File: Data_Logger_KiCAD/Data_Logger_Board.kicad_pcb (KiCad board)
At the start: 6 copper layers, 45 x 63 mm, 105 parts, among them J1 USB_C_Receptacle_USB2.0_16P, J2 Screw_Terminal_01x02, J3 Micro_SD_Card, J4 Conn_Coaxial_Small, J5 Conn_01x02, Q1 Q_NMOS_GSD, SW1 SW_Push, SW2 SW_Push, U1 LSM6DSO32TR, U10 BMP390L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

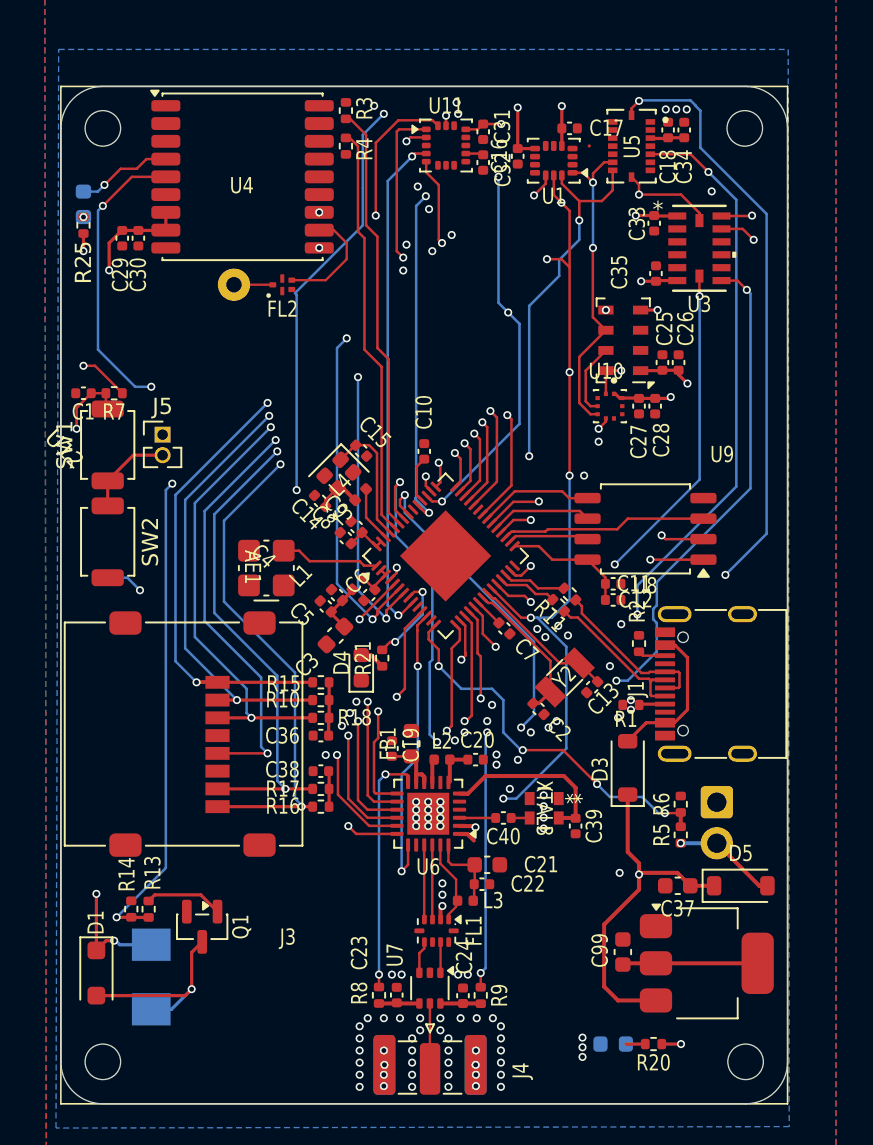
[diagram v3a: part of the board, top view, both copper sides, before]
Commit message: finish SPI routing +silkscreen tidy
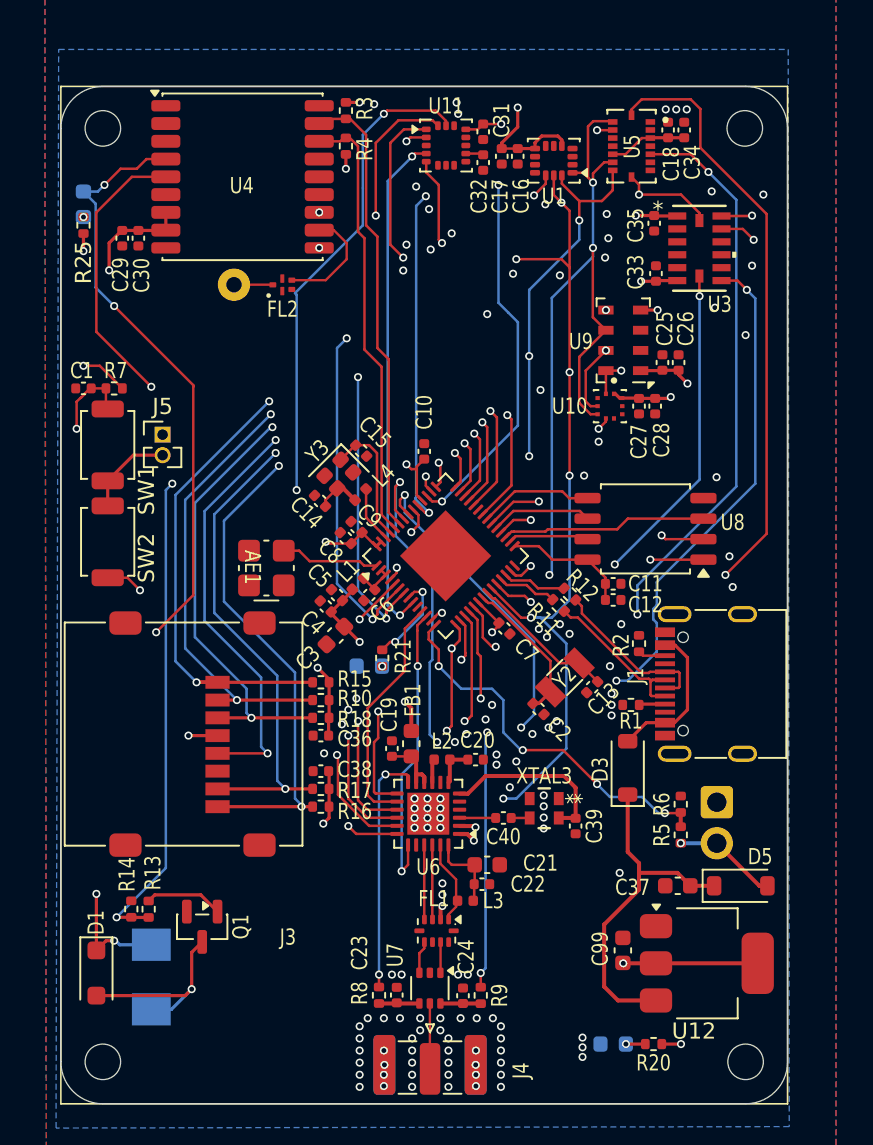
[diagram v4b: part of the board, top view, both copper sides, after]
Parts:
- D4: moved to B.Cu
- moved C17 4.54 mm to (147.3, 51.4), turned to -90 degrees
- moved D4 0.51 mm to (139.1, 83.0), turned to 0 degrees
- moved C1 0.30 mm to (121.4, 65.8)
- moved R7 0.30 mm to (123.3, 65.8)
- moved C99 0.10 mm to (154.8, 100.6)
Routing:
- net /MCU/TIMEPULSE: track 6.08 -> 56.2 mm, vias 1 -> 4
- net /MCU/MISO: track 67.7 -> 101.9 mm, vias 6 -> 8
- net +3V3: track 69.2 -> 85.0 mm, vias 14 -> 24
- net /MCU/MAG_INT: track 31.6 -> 42.3 mm
- net /MCU/MOSI: track 104.5 -> 109.3 mm, vias 7 -> 9
- net /MCU/~{ACCEL_CS}: track 35.9 -> 32.6 mm
- net /MCU/SCL: track 26.6 -> 28.3 mm
- net /MCU/SDA: track 25.5 -> 27.3 mm
- net Net-(D4-A): track 1.59 -> 0.00 mm, vias 0 -> 1
- net /MCU/RADIO_BUSY: track 15.8 -> 14.8 mm, vias 2 -> 0
- net /MCU/PWR_IN: track 21.7 -> 22.4 mm, vias 1 -> 0
- net /MCU/~{RESET}: track 32.1 -> 32.8 mm
- net /MCU/GPS_EXTINT: track 48.2 -> 47.7 mm, vias 3 -> 2
- net /MCU/ACCEL_INT: vias 3 -> 2
- net Net-(U6-VBAT): vias 0 -> 1
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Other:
- board text added: "R12"

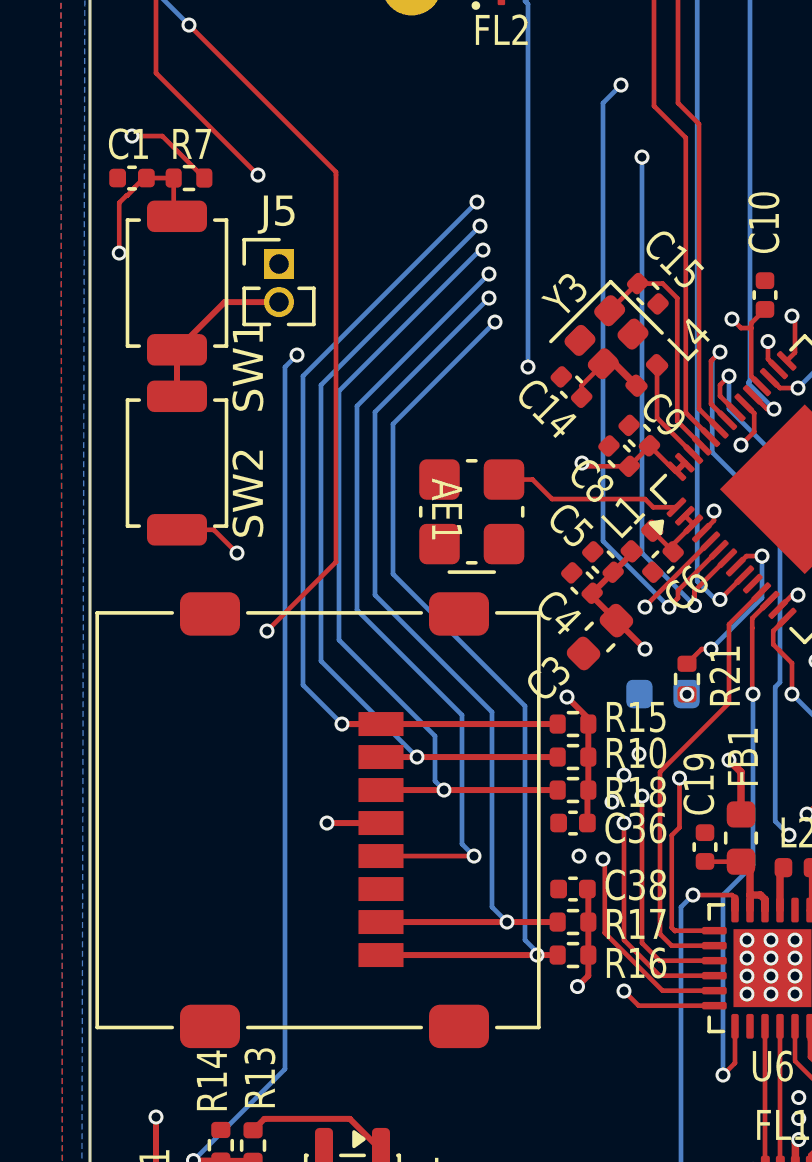
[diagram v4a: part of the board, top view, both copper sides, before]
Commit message: add stitching vias
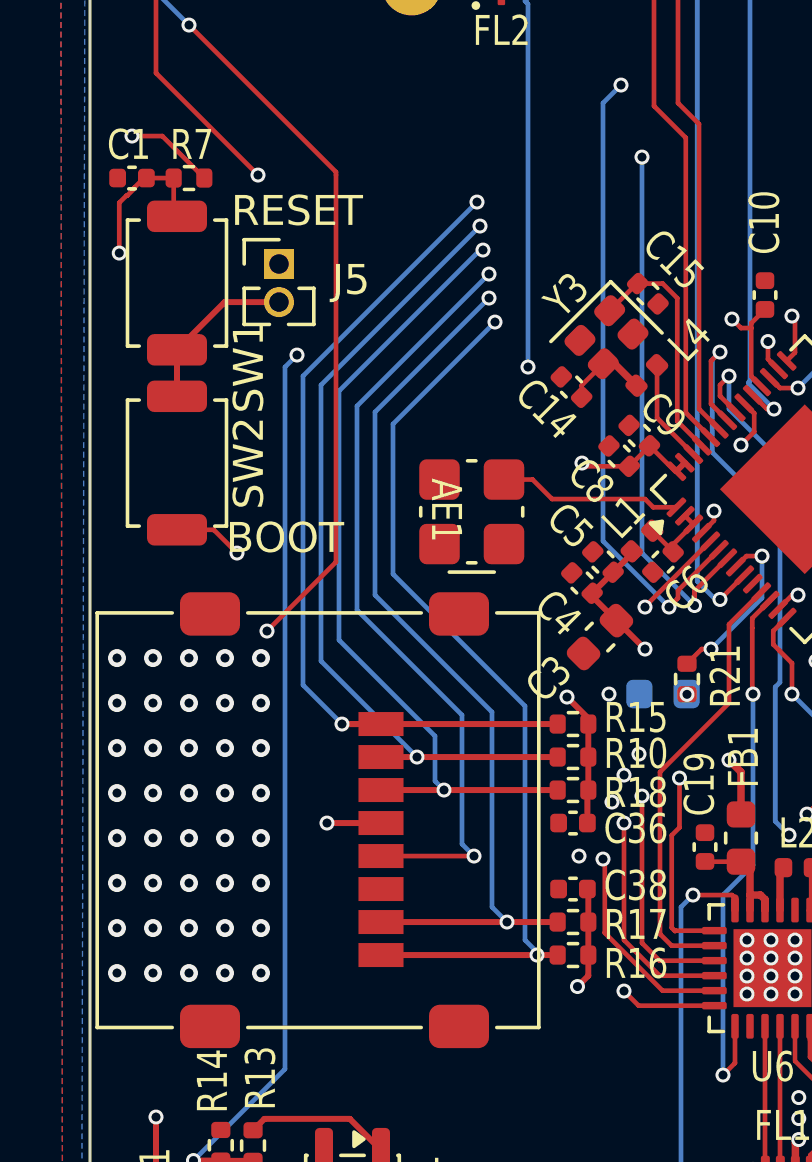
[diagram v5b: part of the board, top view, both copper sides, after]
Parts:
- added REF**: aiaa-mask-silk-8x4, beavs-footprints:aiaa-mask-silk-8x4, B.Cu at (132.3, 106.6)
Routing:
- net GND: vias 124 -> 165
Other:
- board text added: "ASDT"
- board text added: "BOOT"
- board text added: "RESET"

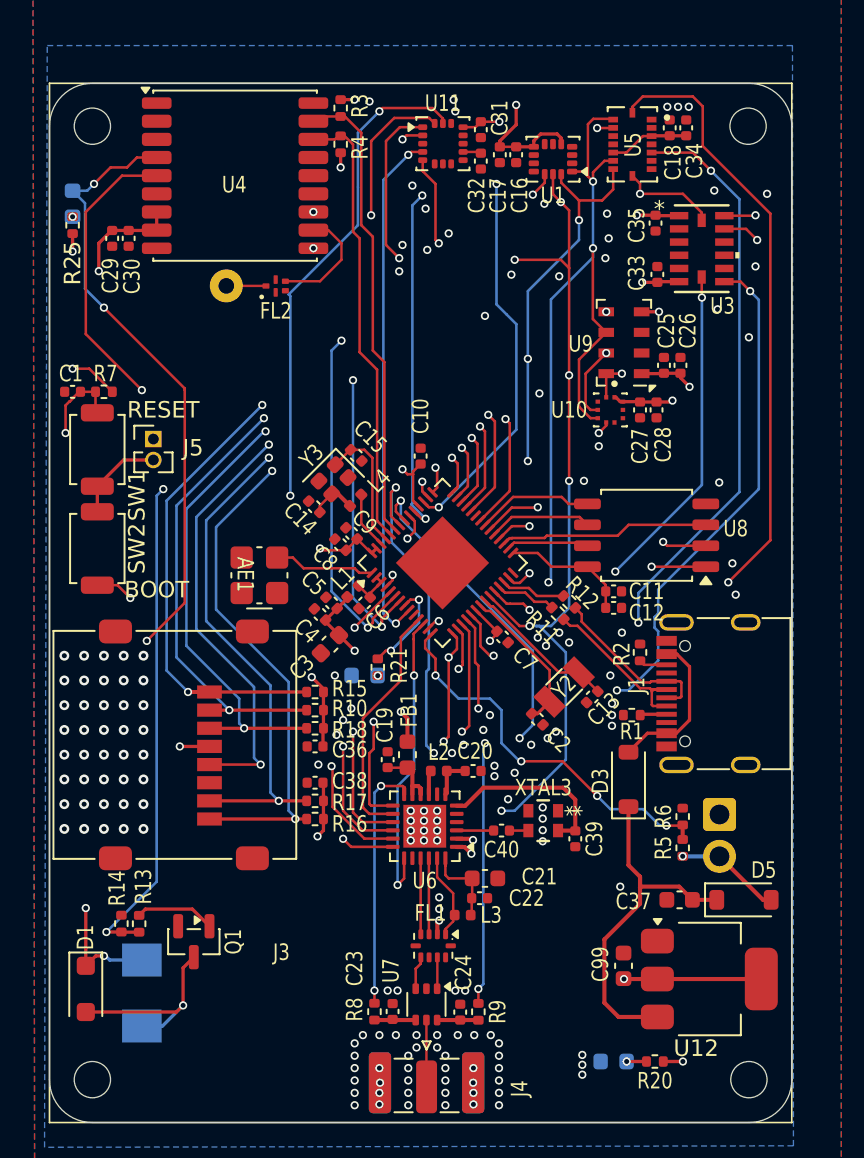
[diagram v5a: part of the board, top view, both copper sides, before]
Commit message: Corrected DRC Errors
Added 220Ohm resistor to TCXO output.
Fixed DRC Errors
Added stitching vias
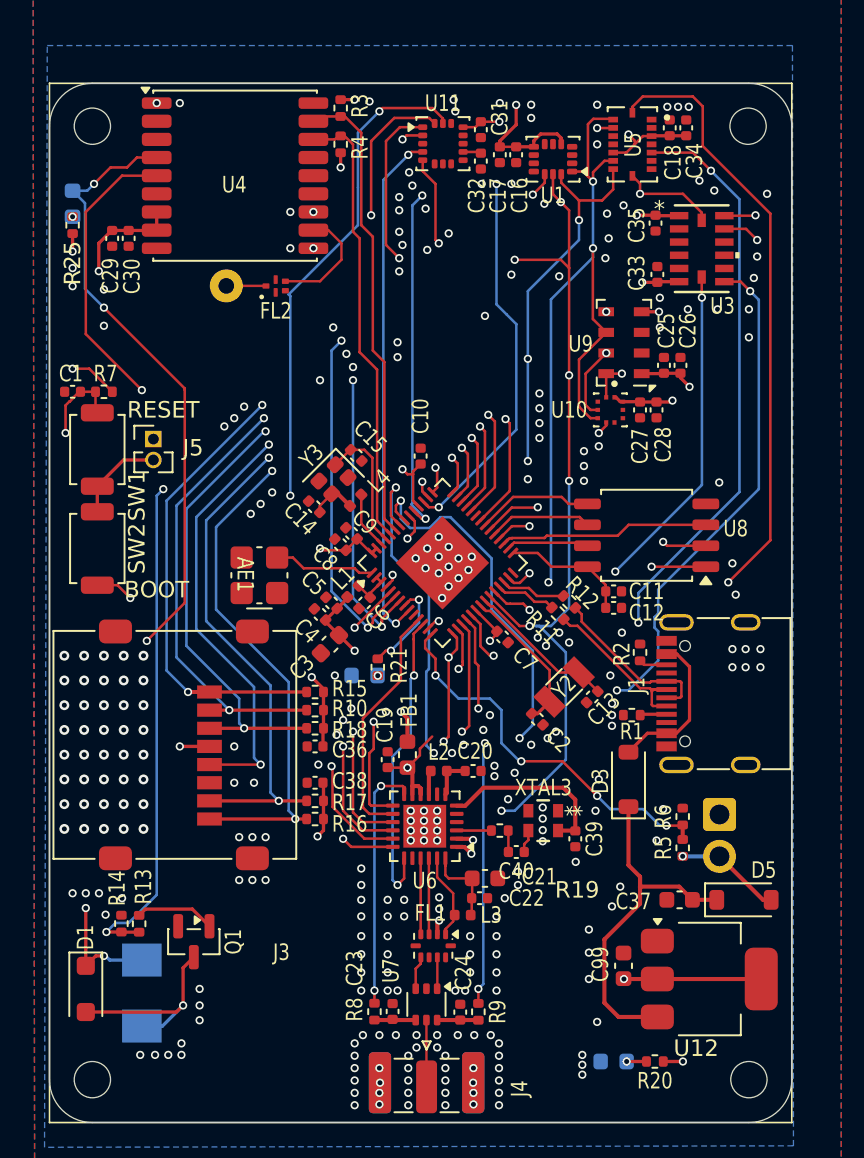
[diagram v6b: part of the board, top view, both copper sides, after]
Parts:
- added R19: 220, Resistor_SMD:R_0402_1005Metric, F.Cu at (147.3, 92.4)
- C40: value 1n -> 10p
- moved C40 1.58 mm to (148.3, 93.7)
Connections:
- C40 pad 2: /MCU/radio/XTA -> Net-(C40-Pad2)
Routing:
- net Net-(U6-VBAT): track 5.27 -> 15.5 mm, vias 1 -> 2
- net /MCU/ANT_SW: track 37.7 -> 40.1 mm
- net Net-(C40-Pad2): track 0.00 -> 1.30 mm
- net +3V3: track 85.0 -> 85.8 mm, vias 24 -> 25
- net GND: vias 165 -> 288
